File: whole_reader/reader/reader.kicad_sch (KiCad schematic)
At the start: 67 parts, among them U1 LM386M-1, U2 STM32F103C8T6, U3 MCP16301Hx-xCH, U4 MAX3232, Y1 16MHz

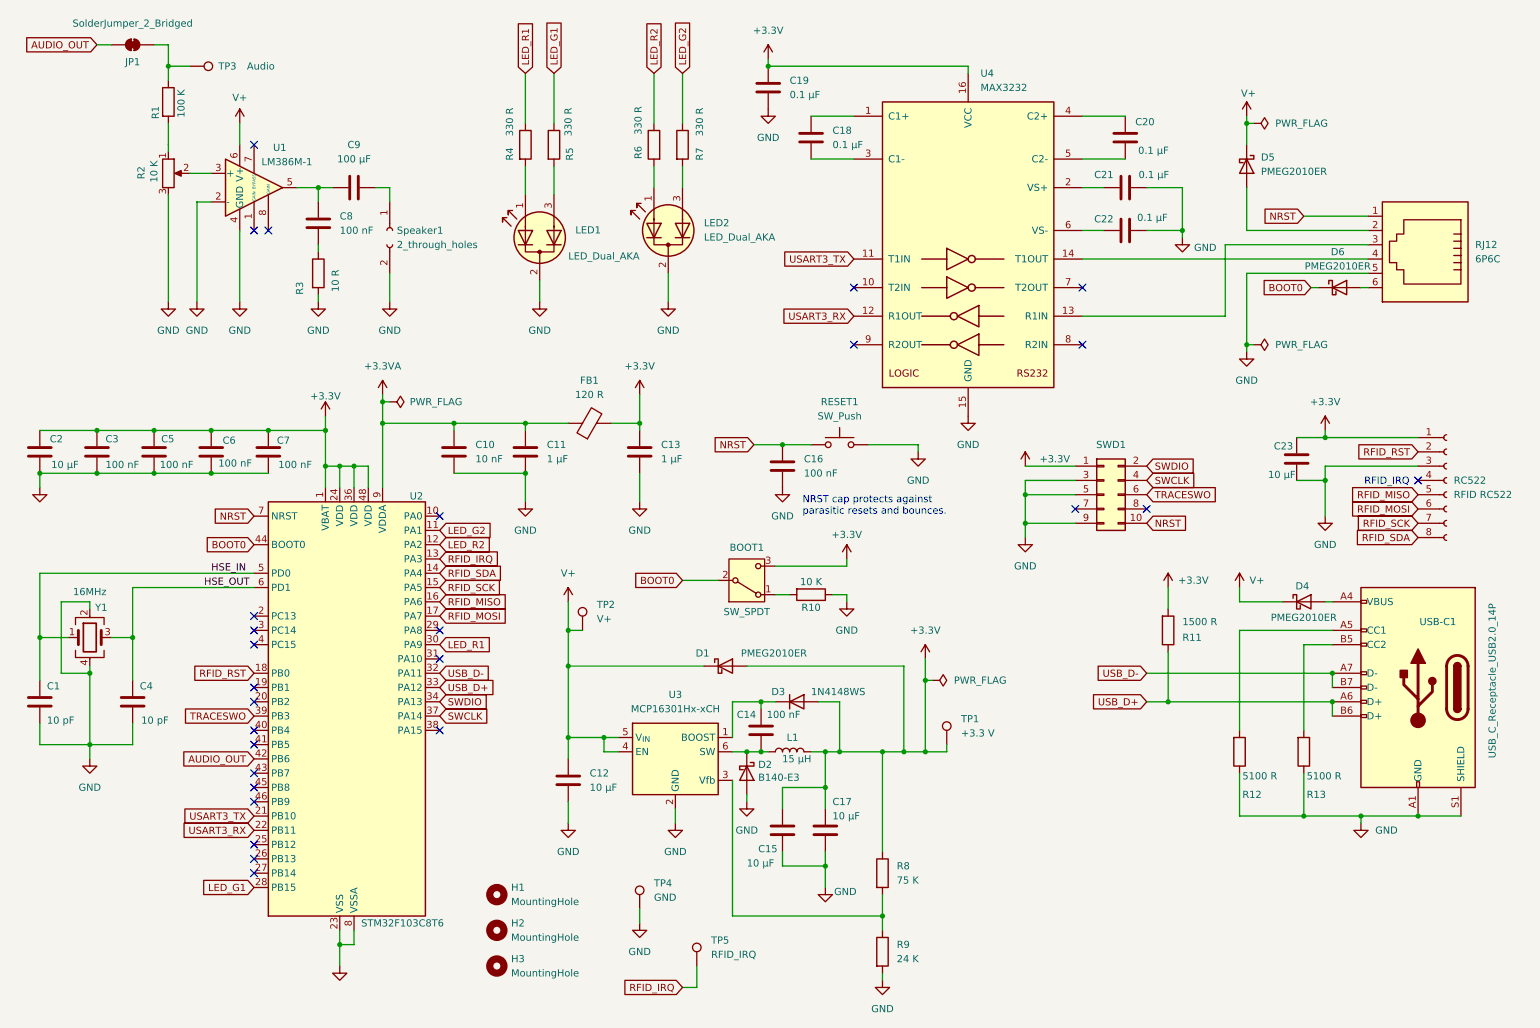
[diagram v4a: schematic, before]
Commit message: Pridanie LCSC, JLSPCB, úprava TP
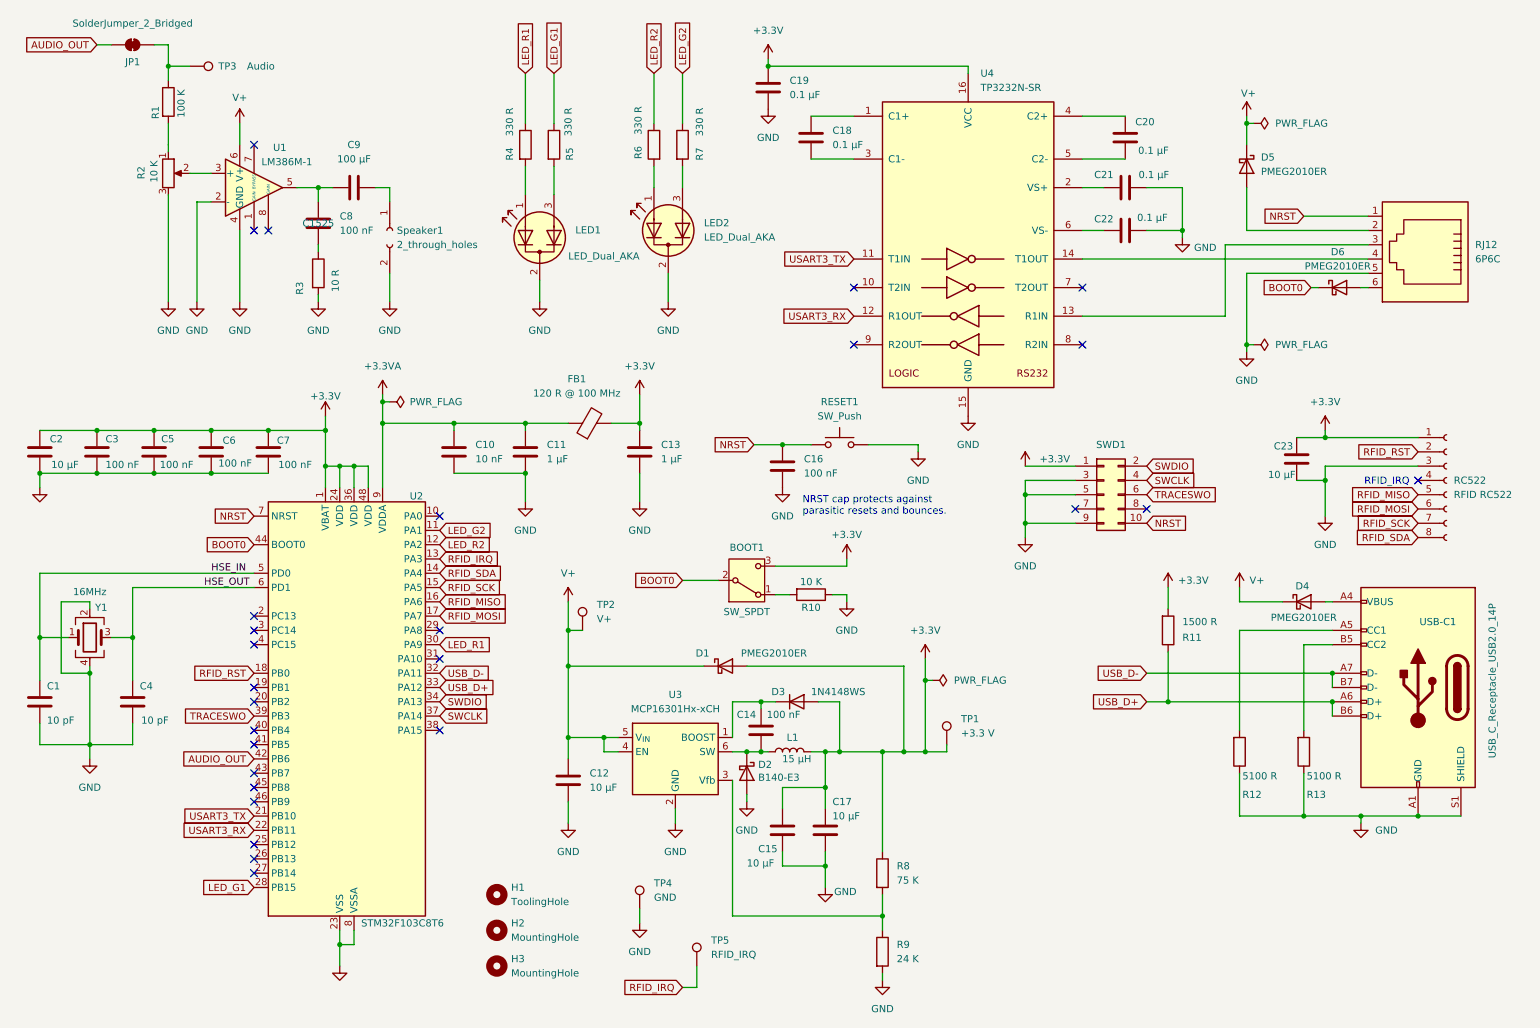
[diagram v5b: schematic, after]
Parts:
- C14, C16, C3, C5, C6, C7, C8: LCSC (none) -> C1525
- FB1: value 120 R -> 120 R @ 100 MHz; JLCPCB (none) -> https://jlcpcb.com/partdetail/Tdk-MMZ1608S121ATD25/C2661467; LCSC (none) -> C2661467; Note (none) -> 150 mΩ ±25% DCR, Current Rating 500 mA
- H1: value MountingHole -> ToolingHole; footprint MountingHole:MountingHole_2.2mm_M2 -> MountingHole:ToolingHole_1.152mm
- H2, H3: footprint MountingHole:MountingHole_2.2mm_M2 -> MountingHole:ToolingHole_1.152mm
- U4: value MAX3232 -> TP3232N-SR; JLCPCB (none) -> https://jlcpcb.com/partdetail/3peak-TP3232NSR/C81661; LCSC (none) -> C81661; Note (none) -> Alternative to MAX3232; Note2 (none) -> https://datasheets.maximintegrated.com/en/ds/MAX3222-MAX324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
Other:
- moved on the sheet: H1

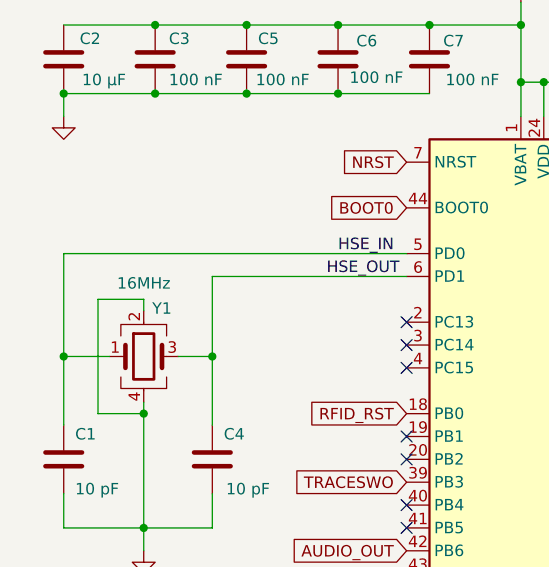
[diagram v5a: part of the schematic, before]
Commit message: Pridaný dátový list a PN pre oscilátor
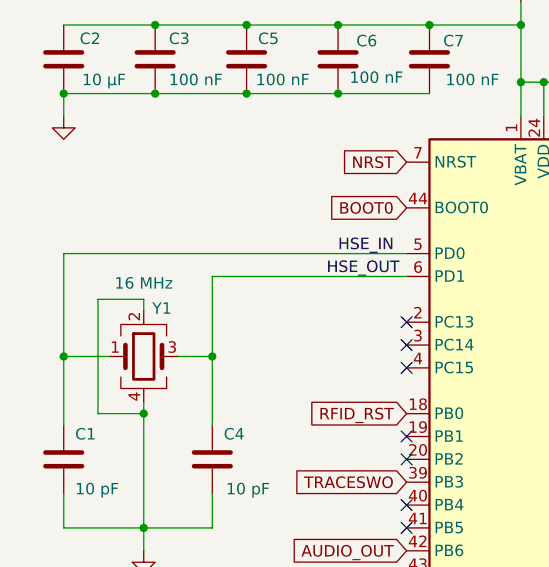
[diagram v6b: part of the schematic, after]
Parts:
- Y1: value 16MHz -> 16 MHz; JLCPCB (none) -> https://jlcpcb.com/partdetail/Yxc_CrystalOscillators-X32251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; LCSC (none) -> C13738; Note (none) -> Load Capacitance 9pF
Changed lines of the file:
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@@
 			"AGwAKwBFAAkACgBwAGMAYgBuAGUAdwAuAFAAaQBjAGsAZQByAC4AcwBlAGwAZQBjAHQASQB0AGUA"
 			"bQBJAG4AdABlAHIAYQBjAHQAaQB2AGUAbAB5AAkACQAKAHAAYwBiAG4AZQB3AC4AUABpAGMAawBl"
-			"AHIALgBzAGUAbABlAGMAdABQAG8AaQBuAA=="
+			"AHIALgBzAGUAbABlAGMAdABQAG8AaQBuAAAAAAAAAAAAAAAAAAAAAAAAAAAAAAAAAAAAAAAAAAAA"
+			"AAAAAAAAAAAAAAAAAAAAAAAAAAAAAAAAAAAAAAAAAAAAAAAAAAAAAAAAAAAAAAAAAAAAAAAAAAAA"
+			"AAAAAAAAAAAAAAAAAAAAAAAAAAAAAAAAAAAAAAAAAAAAAAAAAAAAAAAAAAAAAAAAAAAAAAAAAAAA"
+			"AAAAAAAAAAAAAAAAAAAAAAAAAAAAAAAAAAAAAAAAAAAAAAAAAAAAAAAAAAAAAAAAAAAAAAAAAAAA"
+			"AAAAAAAAAAAAAAAAAAAAAAAAAAAAAAAAAAAAAAAAAAAAAAAAAAAAAAAAAAAAAAAAAAAAAAAAAAAA"
+			"AAAAAAAAAAAAAAAAAAAAAAAAAAAAAAAAAAAAAAAAAAAAAAAAAAAAAAAAAAAAAAAAAAAAAAAAAAAA"
+			"AAAAAAAAAAAAAAAAAAAAAAAAAAAAAAAAAAAAAAAAAAAAAAAAAAAAAAAAAAAAAAAAAAAAAAAAAAAA"
+			"AAAAAAAAAAAAAAAAAAAAAAAAAAAAAAAAAAAAAAAAAAAAAAAAAAAAAAAAAAAAAAAAAAAAAAAAAAAA"
+			"AAAAAAAAAAAAAAAAAAAAAAAAAAAAAAAAAAAAAAAAAAAAAAAAAAAAAAAAAAAAAAAAAAAAAAAAAAAA"
+			"AAAAAAAAAAAAAAAAAAAAAAAAAAAAAAAAAAAAAAAAAAAAAAAAAAAAAAAAAAAAAAAAAAAAAAAAAAAA"
+			"AAAAAAAAAAAAAAAAAAAAAAAAAAAAAAAAAAAAAAAAAAAAAAAAAAAAAAAAAAAAAAAAAAAAAAAAAAAA"
+			"AAAAAAAAAAAAAAAAAAAAAAAAAAAAAAAAAAAAAAAAAAAAAAAAAAAAAAAAAAAAAAAAAAAAAAAAAAAA"
+			"AAAAAAAAAAAAAAAAAAAAAAAAAAAAAAAAAAAAAAAAAAAAAAAAAAAAAAAAAAAAAAAAAAAAAAAAAAAA"
+			"AAAAAAAAAAAAAAAAAAAAAAAAAAAAAAAAAAAAAAAAAAAAAAAAAAAAAAAAAAAAAAAAAAAAAAAAAAAA"
+			"AAAAAAAAAAAAAAAAAAAAAAAAAAAAAAAAAAAAAAAAAAAAAAAAAAAAAAAAAAAAAAAAAAAAAAAAAAAA"
+			"AAAAAAAAAAAAAAAAAAAAAAAAAAAAAAAAAAAAAAAAAAAAAAAAAAAAAAAAAAAAAAAAAAAAAAAAAAAA"
+			"AAAAAAAAAAAAAAAAAAAAAAAAAAAAAAAAAAAAAAAAAAAAAAAAAAAAAAAAAAAAAAAAAAAAAAAAAAAA"
+			"AAAAAAAAAAAAAAAAAAAAAAAAAAAAAAAAAAAAAAAAAAAAAAAAAAAAAAAAAAAAAAAAAAAAAAAAAAAA"
+			"AAAAAAAAAAAAAAAAAAAAAAAAAAAAAAAAAA=="
 		)
 	)
@@
 			"LTQ0YzUtYmNjZS02ZWJkZjkyODNjMjEiKShlZmZlY3RzKGZvbnQoc2l6ZSAxLjI3IDEuMjcpKHRo"
 			"aWNrbmVzcyAwLjE1KSkpKShwcm9wZXJ0eSAiRGVzY3JpcHRpb24iICIyMCBWLCAxIEEgbG93IFZG"
-			"IFNjaG90dGt5IGJhcg=="
+			"IFNjaG90dGt5IGJhcgB3AFgASwA5AGUASABoAC8AdgBnAEMASwBjAFEANgAwAE4AeAB6AGsAVAAw"
+			"AGQATgBRAFcAWgBjAFAAcwBCAEEAQQBBAEEAQQBDAEEAKwBkAFcAYgA0AC8AcgBzAGgAcABhAGEA"
+			"RwA5AHMAYgBFAEcASAA4AGwAWgBjAFkARQBNAGYAUgAyAGMATQBQAGkAQwBOAGYAWgBCAHAAeAAr"
+			"AGoAaQBuAGQATgB1AG4AcwB3AE0AQQBBAEEAQQBBAEEAQgBiAHkAdQArAHkAQQBWAHEAcQB4AFcA"
+			"LwAxAFIAZABnAFMAMABrAHEAMQBsAFAASQAyADQAQQA0ADQAOABJAFoANAA4AHIAaQBGAGQAdAAx"
+			"AG4AWgBQAEQAcwBCAEEAQQBBAEEAQQBHAEEAQgBKAHMAUwBKADgATABGADYAVgBIAFkAQwB0AEYA"
+			"RgA1AFQAVwB5AGMAMwBkAEEAcQBNADAAZgA2ADQASQBnAFQAWQByADAAcQAvAGoAeQArAEwAUgAx"
+			"ADMAUwBDAG4AWgBDAFEAQQBBAEEAQQBBAEEAOAB6AGsANwBPADYAQwBGAEQAcQArAEgAWgBDAGQA"
+			"QQBHADUAVQBTAG4AOABwAHUAYQBKAFcATAA2AHoAVQBqAGYAWABqAGsAVQA0AGcAUgBwADQAeABm"
+			"AEMAYgBGAEIAYgBKADIAZABBAEEAQQBBAEEAQQBBAHcAbgAvAFAAagA3AHUAeQBFAGwAdgBsADIA"
+			"NwBKAFcAZABBAEMAMwAxAGwAbABnAC8ATwA2AEYAVgBSAGoAeQBEAHUAUABnAEoAYwBUAEYALwBP"
+			"AGEAUAAwAHEAVABJAHQATwB3AEUAQQBBAEEAQQBBADQAQgAvAHEAMwBQAGgAVgBkAGsATwByAG4A"
+			"QgBEAHYAcQBqAFUANwBBAHQAcQBvAFQASQA4AEQAcwB4AHQAYQA1AHQAUwBSAFAANwB5ADQAQwBm"
+			"AEYAYwBQADQARQB5AHIAcAA0AFoANwA4ADUATwBBAEEAQQBBAEEAQQBDAFkAegA4ACsAeQBBADEA"
+			"cgBrAHQATgBpADIAegBzADIATwBnAEoAYgBhAFAAWgA2AGUAbgBkAEEAcQBkADgAWgB2AFIAdgA2"
+			"AEUAeABVAHkASQA5AGUARQA0AGYAZgB4AHEAaQBJAGoAOQB5AC8ATABaAEMAUQBBAEEAQQBBAEEA"
+			"QQBqAHoAawBwAG4ASgBvAGIASAA3ACsASgBOADkAZQBIAHMAaQBPAGcAbgBjAG8ASwA4AFkAbgBz"
+			"AGgAcABZADUAcgBjADQAWgArAFIATQBXAGQAdwByAFIAVgBhAGIAagBiAFoAWABZAEoAegBzAEIA"
+			"QQBBAEEAQQBBAE8AQQ=="
 		)
 	)
@@
 			)
 		)
-		(property "Value" "16MHz"
+		(property "Value" "16 MHz"
 			(at 27.94 118.872 0)
 			(effects
@@
 			)
 		)
-		(property "Datasheet" "~"
+		(property "Datasheet" "https://jlcpcb.com/api/file/downloadByFileSystemAccessId/8588879072148017152"
 			(at 27.94 127 0)
 			(effects
@@
 			)
 		)
-		(property "Note" ""
+		(property "Note" "Load Capacitance 9pF"
+			(at 27.94 127 0)
+			(effects
+				(font
+					(size 1.27 1.27)
+				)
+				(hide yes)
+			)
+		)
+		(property "LCSC" "C13738"
 			(at 27.94 127 0)
 			(effects
@@
 					(size 1.27 1.27)
 				)
+				(hide yes)
+			)
+		)
+		(property "JLCPCB" "https://jlcpcb.com/partdetail/Yxc_CrystalOscillators-X322516MLB4SI/C13738"
+			(at 27.94 127 0)
+			(effects
+				(font
+					(size 1.27 1.27)
+				)
+				(hide yes)
 			)
 		)

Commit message: Add files via upload
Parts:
- removed LED1, LED2: LED_Dual_AKA, LED_SMD:LED_Kingbright_KPA-3010_3x2x1mm, symbol Device:LED_Dual_AKA
- added LED1, LED2: LED_Dual_AKKA, LED_SMD:LED_Kingbright_APHBM2012_2x1.25mm, symbol Device:LED_Dual_AKKA
- BOOT1: JLCPCB (none) -> https://jlcpcb.com/partdetail/ck-PCM12SMTR/C221841; LCSC (none) -> C221841
- C1, C4: JLCPCB (none) -> https://jlcpcb.com/partdetail/33914-CL05C100JB5NNNC/C32949; LCSC (none) -> C32949
- C10: JLCPCB (none) -> https://jlcpcb.com/partdetail/15869-CL05B103KB5NNNC/C15195; LCSC (none) -> C15195
- C11, C13, C18, C19, C20, C21, C22: JLCPCB (none) -> https://jlcpcb.com/partdetail/53938-CL05A105KA5NQNC/C52923; LCSC (none) -> C52923
- C12, C15, C17, C2, C23: JLCPCB (none) -> https://jlcpcb.com/partdetail/20411-CL10A106KP8NNNC/C19702; LCSC (none) -> C19702
- C14, C16, C3, C5, C6, C7, C8: JLCPCB (none) -> https://jlcpcb.com/partdetail/1877-CL05B104KO5NNNC/C1525
- C9: JLCPCB (none) -> https://jlcpcb.com/partdetail/152991-GRM21BR60J107ME15L/C14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; LCSC (none) -> C141660
- D1, D4, D5, D6: JLCPCB (none) -> https://jlcpcb.com/partdetail/Nexperia-PMEG2010ER115/C82288; LCSC (none) -> C82288
- D2: JLCPCB (none) -> https://jlcpcb.com/partdetail/VishayIntertech-B140_E361T/C9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; LCSC (none) -> C968568; Note (none) -> 40V 1A 520mV@1A
- D3: JLCPCB (none) -> https://jlcpcb.com/partdetail/2485-1N4148WS/C2128; LCSC (none) -> C2128; Note (none) -> 100V 1.25V@150mA 4ns 150mA
- L1: JLCPCB (none) -> https://jlcpcb.com/partdetail/Coilcraft-LPS3010103MRC/C1927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; LCSC (none) -> C19276043
- R1: JLCPCB (none) -> https://jlcpcb.com/partdetail/Sunway-SC0805J1003F4ANRH/C315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; LCSC (none) -> C3152215
- R10: footprint Resistor_SMD:R_0402_1005Metric -> Resistor_SMD:R_0603_1608Metric; JLCPCB (none) -> https://jlcpcb.com/partdetail/Sunway-SC0603J1002F2BNRH/C315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; LCSC (none) -> C3152154
- R11: JLCPCB (none) -> https://jlcpcb.com/partdetail/26610-0402WGF1501TCE/C25867; LCSC (none) -> C25867
- R12, R13: JLCPCB (none) -> https://jlcpcb.com/partdetail/26648-0402WGF5101TCE/C25905; LCSC (none) -> C25905
- R2: JLCPCB (none) -> https://jlcpcb.com/partdetail/Bourns-3314G_1103E/C780220; LCSC (none) -> C780220; Note (none) -> ±20% ±100ppm/℃ 250mW 10kΩ SMD-3P,4.5x4.5mm
- R3: JLCPCB (none) -> https://jlcpcb.com/partdetail/25882-0402WGJ0100TCE/C25139; LCSC (none) -> C25139
- R4, R5, R6, R7: JLCPCB (none) -> https://jlcpcb.com/partdetail/12862-0402WGJ0331TCE/C12246; LCSC (none) -> C12246
- R8: JLCPCB (none) -> https://jlcpcb.com/partdetail/18507-0805W8F7502T5E/C17819; LCSC (none) -> C17819
- R9: JLCPCB (none) -> https://jlcpcb.com/partdetail/1734-0805W8J0243T5E/C1382; LCSC (none) -> C1382
- RESET1: JLCPCB (none) -> https://jlcpcb.com/partdetail/Bzcn-TSD001A05035A/C2889001; LCSC (none) -> C2889001
- RJ12: JLCPCB (none) -> https://jlcpcb.com/partdetail/AmphenolIcc-54601906WPLF/C435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; LCSC (none) -> C4355015
- U1: JLCPCB (none) -> https://jlcpcb.com/partdetail/slkor_slkormicro_elec-LM386M1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; LCSC (none) -> C5375298
- U2: JLCPCB (none) -> https://jlcpcb.com/partdetail/STMicroelectronics-STM32F103C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; LCSC (none) -> C8734
- U3: JLCPCB (none) -> https://jlcpcb.com/partdetail/MicrochipTech-MCP16301HT_ECH/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; LCSC (none) -> C511272
- USB-C1: JLCPCB (none) -> https://jlcpcb.com/partdetail/5762033-USB4110_GFA/C5143397; LCSC (none) -> C5143397
- Y1: value 16 MHz -> 16MHz; JLCPCB https://jlcpcb.com/partdetail/Yxc_CrystalOscillators-X32251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 -> https://jlcpcb.com/partdetail/Yajingxin-TX322516M4DBDE2T/C5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; LCSC C13738 -> C5310731; Note Load Capacitance 9pF -> 16MHz SMD crystal oscillator 10pF ±10ppm ±30ppm SMD3225-4P 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
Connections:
- net GND: now also LED1.2 (K1), LED1.3 (K2), LED2.2 (K1), LED2.3 (K2)
- net LED_G1: now also R4.1; no longer R5.1
- net LED_G2: now also R6.1; no longer R7.1
- net LED_R1: now also R5.1; no longer R4.1
- net LED_R2: now also R7.1; no longer R6.1
- net at R4.2: now also LED1.4 (A2)
- net at R6.2: now also LED2.4 (A2)
- net at R7.2: now also LED2.1 (A1)
- net at R5.2: now also LED1.1 (A1)

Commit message: STM32 datasheet, drobné úpravy PCB
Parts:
- LED1: LCSC C6465979 -> C6465979
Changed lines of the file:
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@@
 			"//////+90dv//////73R2///////vNDakf////+229sHAAAAAAAAAAAAAAAAAAAAAAAAAAAAAAAA"
 			"AAAAAAAAAAAAAAAAAAAAAAAAAAAAAAAAAAAAAAAAAAAAAAAAAAAAAAAAAAAAAAAAAAAAAAAAAAAA"
+			"AAAAAAAAAAAAAAAAAAAAAAAAAAAAAAAAAAAAAAAAAAAAAAAAAAAAAAAAAAAAAAAAAAAAAAAAAAAA"
+			"AAAAAAAAAAAAAAAAAAAAAAAAAAAAAAAAAAAAAAAAAAAAAAAAAAAAAAAAAAAAAAAAAAAAAAAAAAAA"
+			"AAAAAAAAAAAAAAAAAAAAAAAAAAAAAAAAAAAAAAAAAAAAAAAAAAAAAAAAAAAAAAAAAAAAAAAAAAAA"
+			"AAAAAAAAAAAAAAAAAAAAAAAAAAAAAAAAAAAAAAAAAAAAAAAAAAAAAAAAAAAAAAAAAAAAAAAAAAAA"
+			"AAAAAAAAAAAAAAAAAAAAAAAAAAAAAAAAAAAAAAAAAAAAAAAAAAAAAAAAAAAAAAAAAAAAAAAAAAAA"
+			"AAAAAAAAAAAAAAAAAAAAAAAAAAAAAAAAAAAAAAAAAAAAAAAAAAAAAAAAAAAAAAAAAAAAAAAAAAAA"
+			"AAAAAAAAAAAAAAAAAAAAAAAAAAAAAAAAAAAAAAAAAAAAAAAAAAAAAAAAAAAAAAAAAAAAAAAAAAAA"
+			"AAAAAAAAAAAAAAAAAAAAAAAAAAAAAAAAAAAAAAAAAAAAAAAAAAAAAAAAAAAAAAAAAAAAAAAAAAAA"
+			"AAAAAAAAAAAAAAAAAAAAAAAAAAAAAAAAAAAAAAAAAAAAAAAAAAAAAAAAAAAAAAAAAAAAAAAAAAAA"
+			"AAAAAAAAAAAAAAAAAAAAAAAAAAAAAAAAAAAAAAAAAAAAAAAAAAAAAAAAAAAAAAAAAAAAAAAAAAAA"
+			"AAAAAAAAAAAAAAAAAAAAAAAAAAAAAAAAAAAAAAAAAAAAAAAAAAAAAAAAAAAAAAAAAAAAAAAAAAAA"
+			"AAAAAAAAAAAAAAAAAAAAAAAAAAAAAAAAAAAAAAAAAAAAAAAAAAAAAAAAAAAAAAAAAAAAAAAAAAAA"
+			"AAAAAAAAAAAAAAAAAAAAAAAAAAAAAAAAAAAAAAAAAAAAAAAAAAAAAAAAAAAAAAAAAAAAAAAAAAAA"
+			"AAAAAAAAAAAAAAAAAAAAAAAAAAAAAAAAAAAAAAAAAAAAAAAAAAAAAAAAAAAAAAAAAAAAAAAAAAAA"
+			"AAAAAAAAAAAAAAAAAAAAAAAAAAAAAAAAAAAAAAAAAAAAAAAAAAAAAAAAAAAAAAAAAAAAAAAAAAAA"
+			"AAAAAAAAAAAAAAAAAAAAAAAAAAAAAAAAAAAAAAAAAAAAAAAAAAAAAAAAAAAAAAAAAAAAAAAAAAAA"
+			"AAAAAAAAAAAAAAAAAAAAAAAAAAAAAAAAAAAAAAAAAAAAAAAAAAAAAAAAAAAAAAAAAAAAAAAAAAAA"
+			"AAAAAAAAAAAAAAAAAAAAAAAAAAAAAAAAAAAAAAAAAAAAAAAAAAAAAAAAAAAAAAAAAAAAAAAAAAAA"
 			"AAAAAAAAAAAAAAAAAAAAAAAAAAAAAAAAAA=="
 		)
@@
 			"ZgAAAFgAAABGAAAAegAAAHIAAABsAAAAeAAAAGwAAAB1AAAAaAAAAEEAAABUAAAAWQAAAHIAAAAy"
 			"AAAARAAAAHMAAAB3AAAATwAAAGEAAAA1AAAAUgAAAFIAAABpAAAATAAAAFIAAABNAAAAaQAAAHoA"
-			"AABUAAAASQAAAGgAAA=="
+			"AABUAAAASQAAAGgAAAIAAgAAAAlKAAAE/wABCY4CAAIAABMFIwAQAwIBAAm5AAACAAAVB8MAAAQB"
+			"AAEJPgIAAgAAFAZzABADAgERCQ8AAAIAAAAJIQAABP8AAQl+AgACAAAUBlMAEAMCAQAJ6AAAAgAA"
+			"AAkHAAAEAQABCV4CAAIAABMHMwAQAwIBAQkeAgACAAAACWIAAAT/AAEJngIAAgAAEwUjABADAgEA"
+			"CawAAAIAABUHowAABAEAAQk2AgACAAAUBmMAEAMCAQAJ/QAAAgAAAAkXAAAE/wABCXYCAAIAABQG"
+			"QwAQAwIBAAnZAAACAAAACQMAAAQBAAEJVgIAAgAAEwcrABADAgEBCRYCAAIAAAAJVAAABP8AAQmW"
+			"AgACAAATBSMAEAMCAQAJxAAAAgAAEggTAAAEAQABCUYCAAIAABQGcwAQAwIBAQkGAgACAAAACS8A"
+			"AAT/AAEJhgIAAgAAFAZTABADAgEACe8AAAIAAAAJDgAABAEAAQlmAgACAAATBzsAEAMCAQEJJgIA"
+			"AgAAAAmYAAAE/wACCagCAAIAABMFIwAQAwIBAAmhAAACAAAVB4MAAAQBAAEJLAIAAgAAFAZjABAD"
+			"AgEACfUAAAIAAAAJEQAABP8AAQlsAgACAAAUBkMAEAMCAQAJyAAAAgAAEggXAAAEAQABCUwCAAIA"
+			"ABIHHwAQAwIBAQkMAgACAAAACTgAAAT/AAEJjAIAAgAAEwUjABADAgEACbgAAAIAABUHwwAABAEA"
+			"AQk8AgACAAAUBnMAEAMCAREJDQAAAgAAAAkgAAAE/wABCXwCAAIAABQGUwAQAwIBAAniAAACAAAA"
+			"CQYAAAQBAAEJXAIAAgAAEwczABADAgEBCRwCAAIAAAAJWAAABP8AAQmcAgACAAATBSMAEAMCAQAJ"
+			"qwAAAgAAFQejAAAEAQABCTQCAAIAABQGYwAQAwIBAAn8AAACAAAACRYAAAT/AAEJdAIAAgAAFAZD"
+			"ABADAgEACdYAAAIAABUI4wAABAEAAQlUAgACAAATBysAEAMCAQEJFAIAAgAAAAlTAAAE/wABCZQC"
+			"AAIAABMFIwAQAwIBAAnCAAACAAAACAIAAAQBAAEJRAIAAgAAFAZzABADAgEBCQQCAAIAAAAJKgAA"
+			"BP8AAQmEAgACAAAUBlMAEAMCAQAJ7gAAAgAAAAkMAAAEAQABCWQCAAIAABMHOwAQAwIBAQkkAgAC"
+			"AAAACZYAAAT/AAIJpAIAAgAAEwUjABADAgEACagAAAIAABUHgwAABAEAAQkwAgACAAAUBmMAEAMC"
+			"AQAJ+gAAAgAAAAkUAAAE/wABCXACAAIAABQGQwAQAwIBAAnQAAACAAASCBsAAAQBAAEJUAIAAgAA"
+			"EgcfABADAgEBCRACAA=="
 		)
 	)
@@
 		(dnp no)
 		(property "Reference" "U2"
-			(at 84.836 101.854 0)
+			(at 81.788 98.298 0)
 			(effects
 				(font
@@
 		)
 		(property "Value" "STM32F103C8T6"
-			(at 76.2 177.8 0)
+			(at 81.788 100.838 0)
 			(effects
 				(font
@@
 			)
 		)
-		(property "Datasheet" "https://www.st.com/resource/en/datasheet/stm32f103c8.pdf"
+		(property "Datasheet" "https://jlcpcb.com/api/file/downloadByFileSystemAccessId/8579708215774674944"
 			(at 72.39 140.97 0)
 			(effects
@@
 			)
 		)
-		(property "Description" "STMicroelectronics Arm Cortex-M3 MCU, 64KB flash, 20KB RAM, 72 MHz, 2.0-3.6V, 37 GPIO, LQFP48"
+		(property "Description" "STM Arm Cortex-M3 MCU, 64KB Flash, 20KB SRAM, 72 MHz, 2.0-3.6V, 37 GPIO, LQFP48"
 			(at 72.39 140.97 0)
 			(effects
@@
 			)
 		)
-		(property "LCSC" "    C6465979"
+		(property "LCSC" "C6465979"
 			(at 107.95 55.88 0)
 			(effects
